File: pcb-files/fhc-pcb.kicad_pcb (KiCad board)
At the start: 2 copper layers, 133.3 x 63.5 mm, 22 parts, among them J1 Screw_Terminal_01x02, SW1 SW_Push_Dual, SW2 SW_Push_Dual, SW3 SW_Push_Dual, SW4 SW_Push_Dual, SW5 SW_Push_Dual, SW7 SW_Push, U1 WeMos_D1_mini, U3 OLED_0.91_AZDelivery

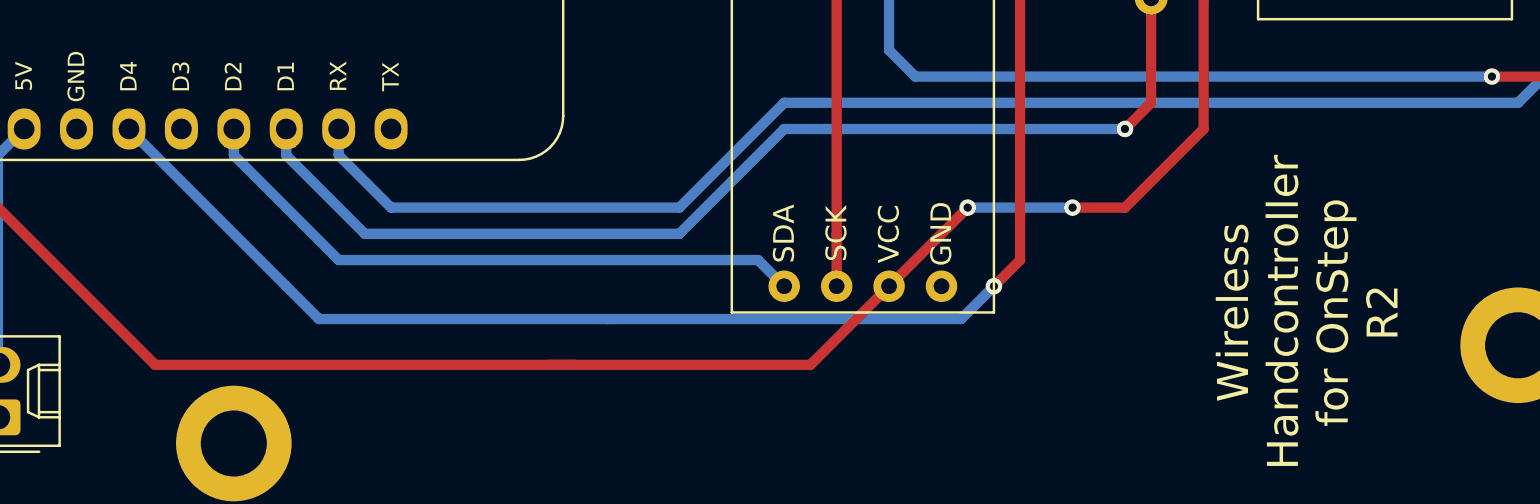
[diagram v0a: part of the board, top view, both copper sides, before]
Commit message: PCB: put status LED on D3
Moved from D4 (decouple from onboard LED)
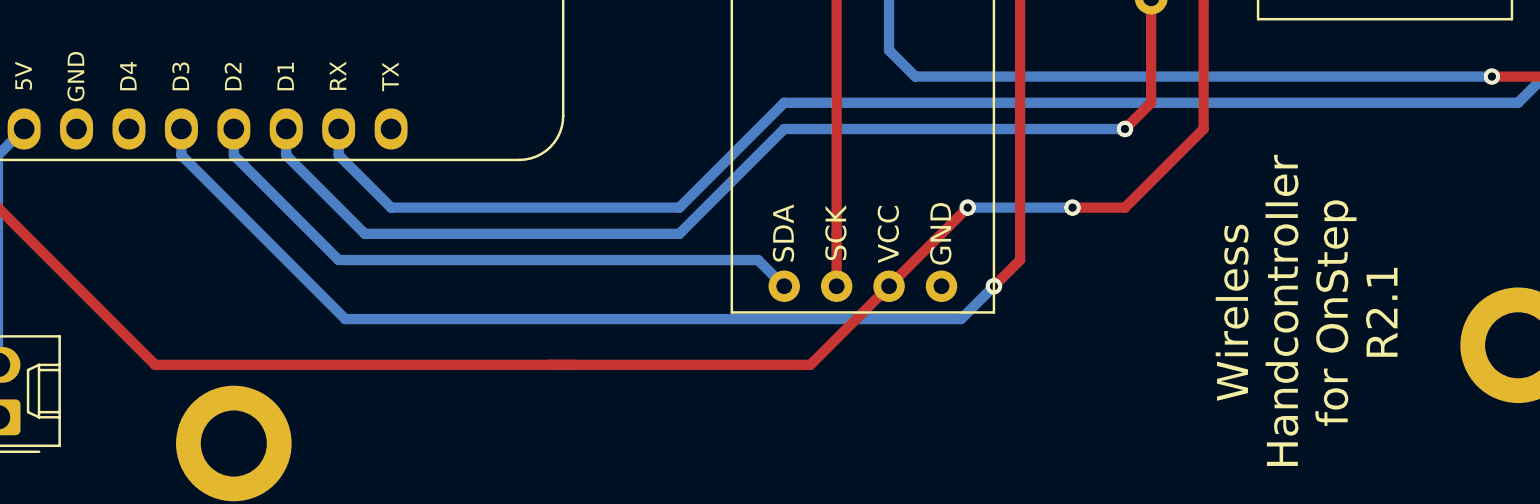
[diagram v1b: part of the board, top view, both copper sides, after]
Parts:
- D1: value LED -> LED_RED_2.1V
- R6: value 150 -> 3.3k
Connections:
- U1 pad 11: Net-(D1-Pad1) -> Net-(U1-Pad11)
- U1 pad 12: Net-(U1-Pad12) -> Net-(D1-Pad1)
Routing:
- net Net-(D1-Pad1): track 99.7 -> 98.0 mm
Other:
- board text added: "Wireless Handcontroller for OnStep R2.1"
- board text removed: "Wireless Handcontroller for OnStep R2"
